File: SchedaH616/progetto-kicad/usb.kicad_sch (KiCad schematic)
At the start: 11 parts, among them J801 903-131A1011D10100, U801 TPS2553DBVR, U802 USBLC6-2SC6

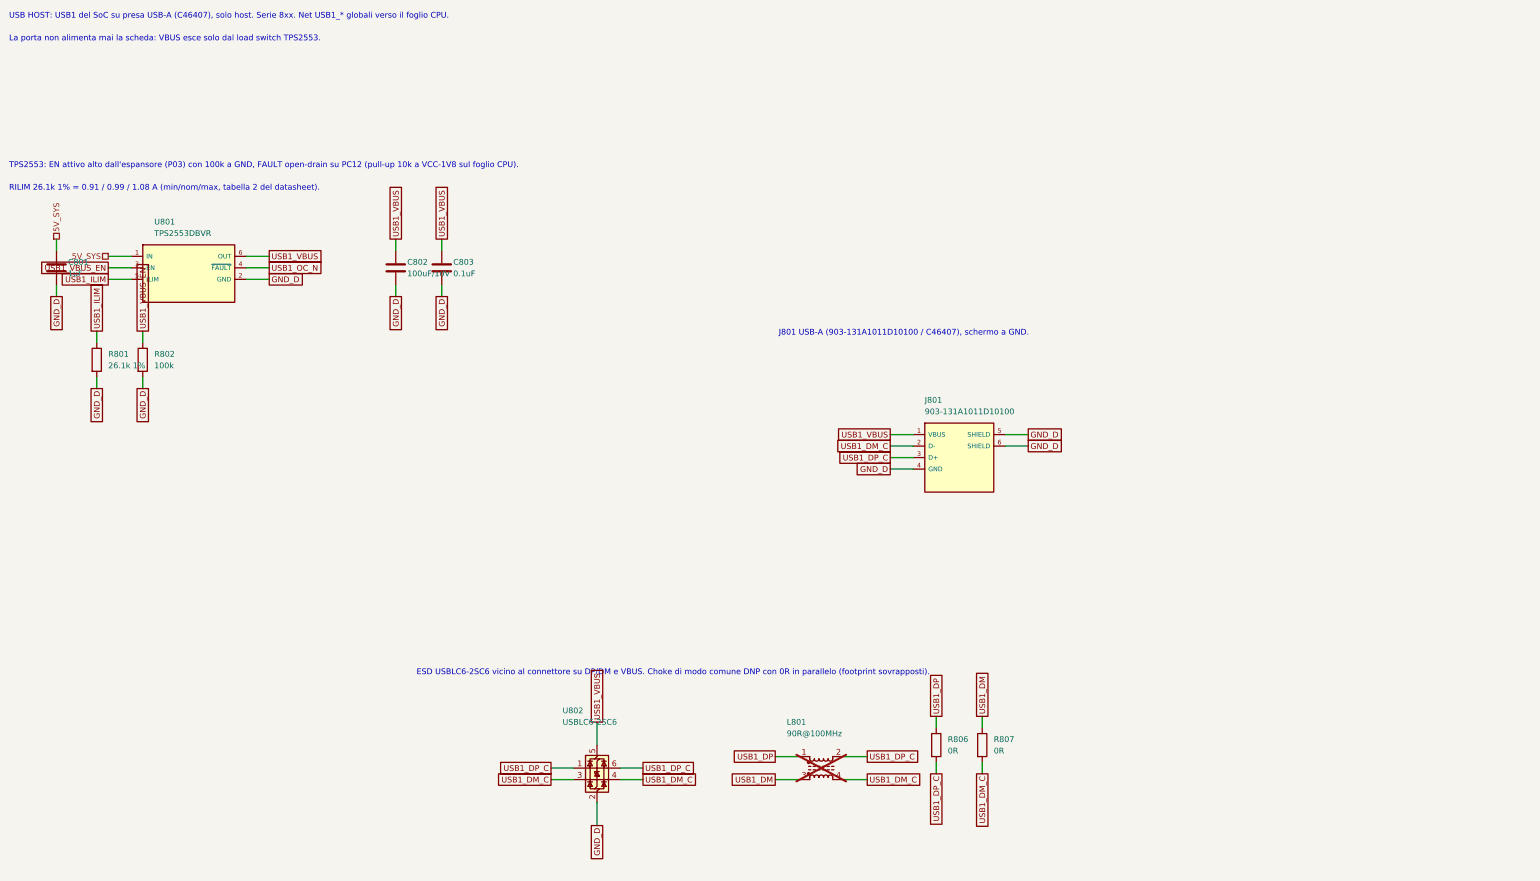
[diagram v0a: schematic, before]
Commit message: SchedaH616: placement PCB 50x70 a 6 strati e modifiche allo schema
PCB (solo placement, niente piste), generato da generatori/build_pcb.sh:
- 50 x 70 mm, smussi 3 mm, 4 fori NPTH 2.2 mm con keepout, 6 strati
- H616 al centro, LPDDR4 sul lato DRAM, AXP313A vicino alla CPU, eMMC vicino ai pin PC
- connettori sui bordi, U.FL Wi-Fi e SMA GNSS su lati opposti
- disaccoppiamento di H616 e LPDDR4 sul bottom sotto le sfere
- regole: piste 5 mil, via-in-pad 0.25/0.15 sotto l'H616
- DRC: 0 violazioni (solo collegamenti da fare), parità schema/PCB ok

Schema (modifiche approvate):
- LPDDR4 confermata come scelta definitiva
- USB host di nuovo su USB-C solo host (Rp 22k, USBLC6-2, TPS2553)
- jack 5 V diretto su IN1 del TPS2121, tolto l'SS54, TPS56637 in Eco-mode
- LDO AP2112K-1.8 (C176944) dedicato a VCCQ eMMC e VCC_PC
- ERC 0

Libreria H616.pretty: serigrafia sui pad tolta, pioli di centraggio NPTH.

Co-Authored-By: Claude Opus 5.5 (1M context) <noreply@anthropic.com>
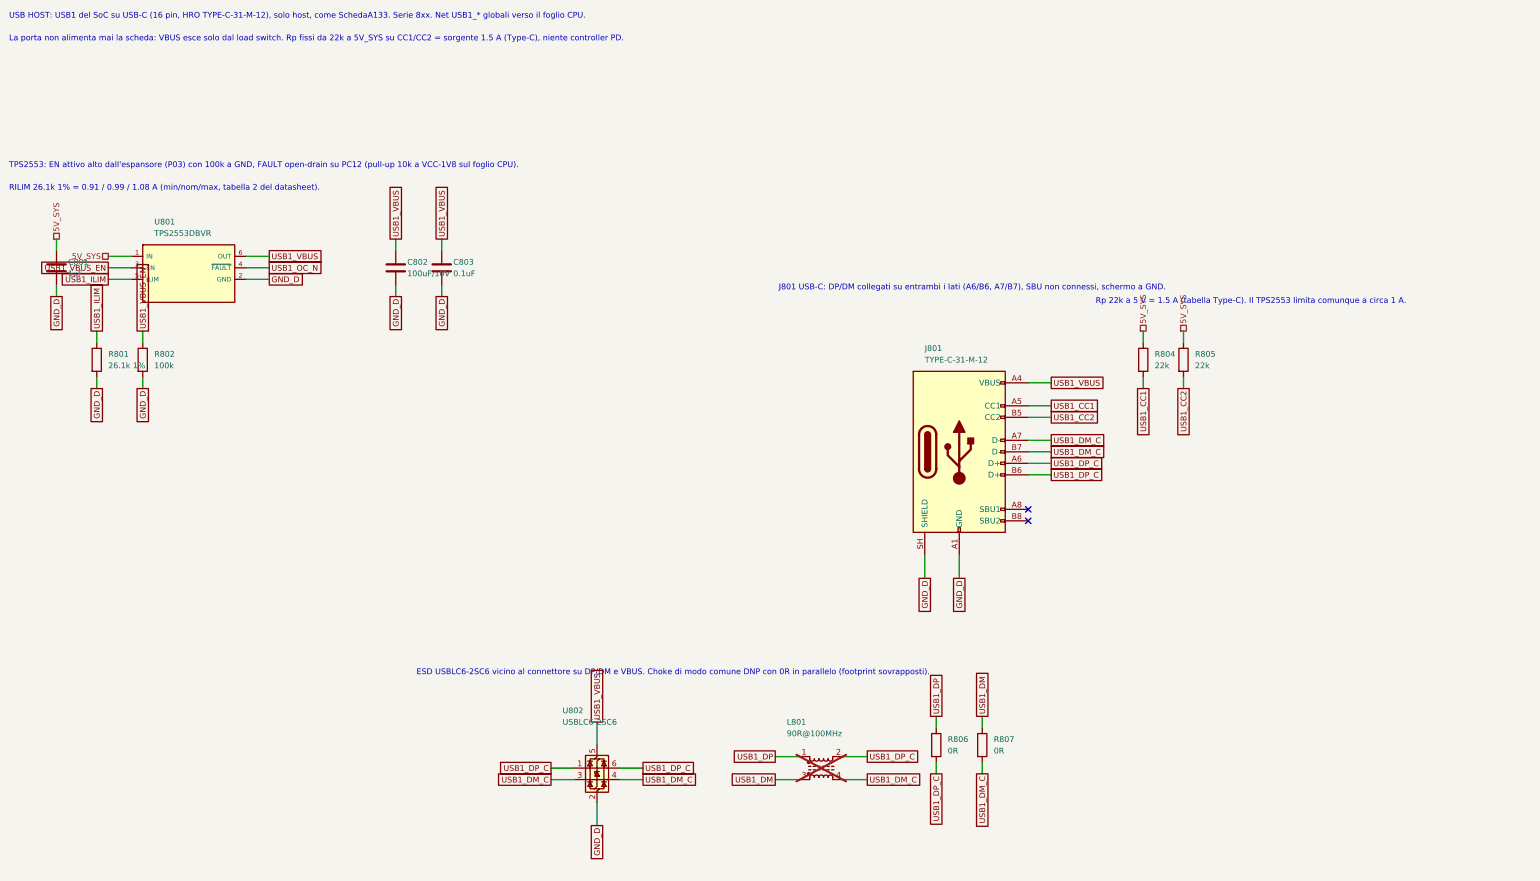
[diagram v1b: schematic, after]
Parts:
- removed J801: 903-131A1011D10100, H616:USB-A-TH_C46407, symbol H616:USB_A_C46407
- added J801: TYPE-C-31-M-12, Connector_USB:USB_C_Receptacle_HRO_TYPE-C-31-M-12, symbol Connector:USB_C_Receptacle_USB2.0_16P
- added R804, R805: 22k, Resistor_SMD:R_0402_1005Metric, symbol Device:R
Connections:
- net 5V_SYS: now also R804.1, R805.1
- net GND_D: now also J801.A1 (GND), J801.A12 (GND), J801.B1 (GND), J801.B12 (GND), J801.SH (SHIELD)
- net USB1_DM_C: now also J801.A7 (D-), J801.B7 (D-)
- net USB1_DP_C: now also J801.A6 (D+), J801.B6 (D+)
- net USB1_VBUS: now also J801.A4 (VBUS), J801.A9 (VBUS), J801.B4 (VBUS), J801.B9 (VBUS)
- new net USB1_CC1: J801.A5 (CC1), R804.2
- new net USB1_CC2: J801.B5 (CC2), R805.2
- no-connect marks 0 -> 2
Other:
- note added: "J801 USB-C: DP/DM collegati su entrambi i lati (A6/B6, A7/B7), SBU non connessi, schermo a GND."
- note added: "La porta non alimenta mai la scheda: VBUS esce solo dal load switch. Rp fissi da 22k a 5V_SYS su CC1/CC2 = sorgente 1.5 A (Type-C), niente controller PD."
- note added: "Rp 22k a 5 V = 1.5 A (tabella Type-C). Il TPS2553 limita comunque a circa 1 A."
- note added: "USB HOST: USB1 del SoC su USB-C (16 pin, HRO TYPE-C-31-M-12), solo host, come SchedaA133. Serie 8xx. Net USB1_* globali verso il foglio CPU."
- note removed: "J801 USB-A (903-131A1011D10100 / C46407), schermo a GND."
- note removed: "La porta non alimenta mai la scheda: VBUS esce solo dal load switch TPS2553."
- note removed: "USB HOST: USB1 del SoC su presa USB-A (C46407), solo host. Serie 8xx. Net USB1_* globali verso il foglio CPU."

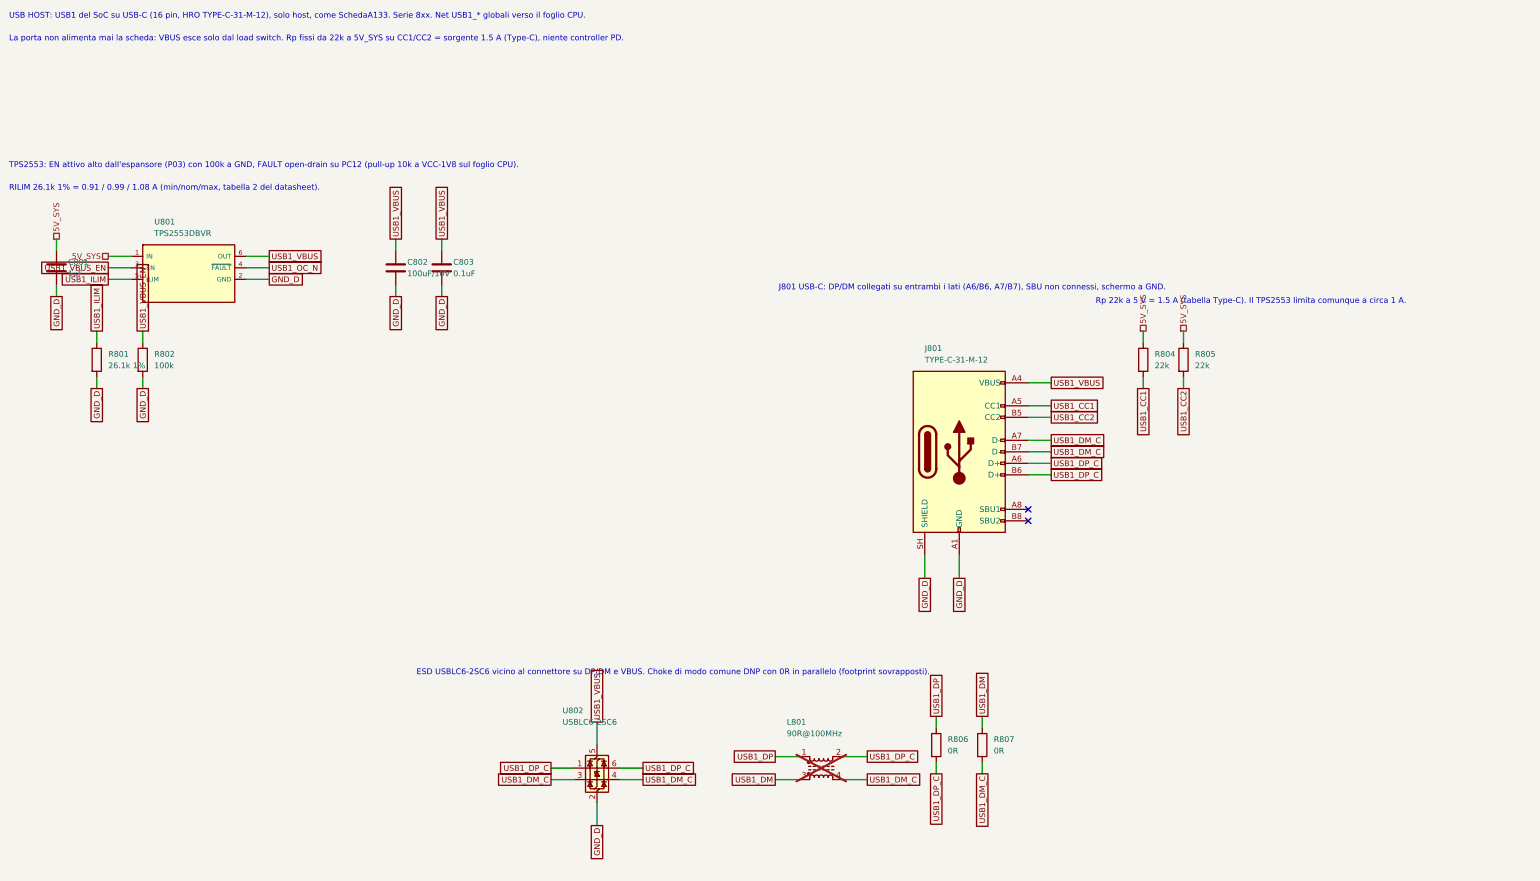
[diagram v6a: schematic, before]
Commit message: SchedaH616: RK3568 + RK809-5 + TCS4525 + DDR4, placement 50x70
- SoC Allwinner H616 -> Rockchip RK3568 (FCBGA636L, LCSC C2938930): ball map dal pinout
  Rockchip V1.1, verificata sulla tabella 2-1 del datasheet V1.2 (636/636); footprint
  generato (gen_fp.py), confrontato con EasyEDA C2938930
- PMIC AXP313A -> RK809-5 (C2939628) come Rockchip AIoT REF V1.1 / ROCK 3A; TCS4525 per
  VDD_CPU su I2C0 (0x1C); BUCK4 su VDD_NPU (sull'RK809-5 parte spento: non puo' fare il 3.3 V)
- LPDDR4 -> DDR4 x16 K4AAG165WA-BCWE (C2920140) sul canale A, point-to-point, niente VTT,
  VPP da AP2112K-2.5, ZQ 240R, DDR_RZQ del SoC 120R (Hardware Design Guide)
- eMMC su EMMC 8 bit (VCCIO2 1.8 V), microSD su SDMMC0, AP6256 su SDMMC2 + UART8,
  RTL8211F su GMAC0 RGMII (22R TX al SoC e RX al PHY), console UART2_M0, USB-C su OTG0
- Recovery su SARADC_VIN0, reset sulla rete RESETn; TCA6416A tolto
- Bus MIKILAB: BUS_POWER su SPI3_M1, MAIN su SPI2_M1 (CS del DAC su cs-gpios)
- progetto rinominato SchedaRK3568, libreria di progetto Scheda; script portabili Linux/macOS
- ERC 0, parita' 0, DRC 0 (solo collegamenti da fare); placement 439/439

Co-Authored-By: Claude Opus 5.5 (1M context) <noreply@anthropic.com>
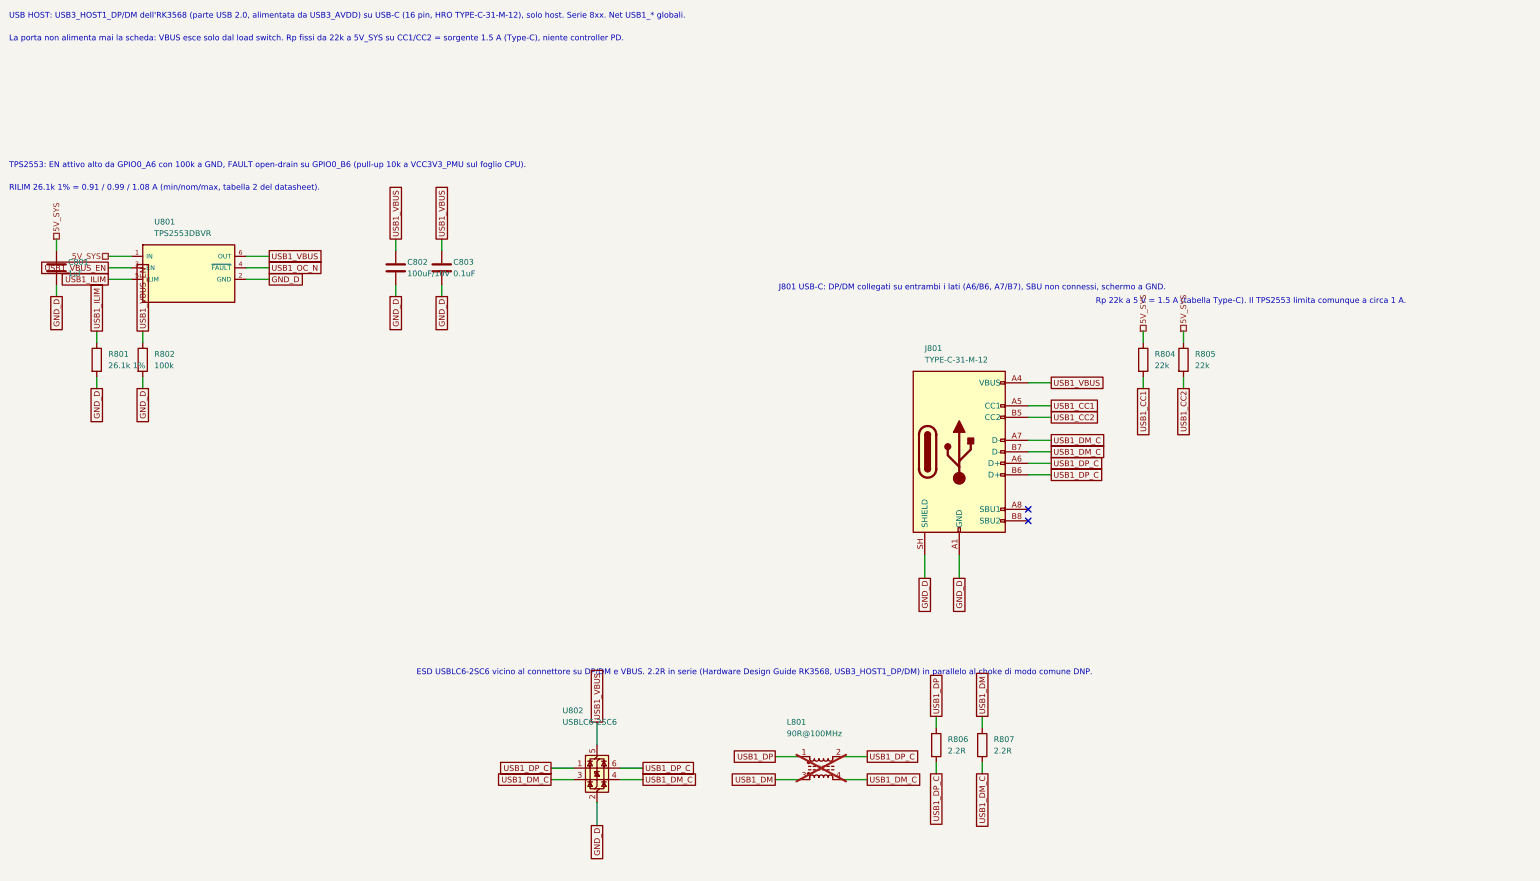
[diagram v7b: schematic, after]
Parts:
- removed U801: TPS2553DBVR, Package_TO_SOT_SMD:SOT-23-6, symbol H616:TPS2553DBV
- added U801: TPS2553DBVR, Package_TO_SOT_SMD:SOT-23-6, symbol Scheda:TPS2553DBV
- R806, R807: value 0R -> 2.2R
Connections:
- net 5V_SYS: now also U801.1 (IN)
- net GND_D: now also U801.2 (GND)
- net USB1_ILIM: now also U801.5 (ILIM)
- net USB1_OC_N: now also U801.4 (~{FAULT})
- net USB1_VBUS: now also U801.6 (OUT)
- net USB1_VBUS_EN: now also U801.3 (EN)
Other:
- note added: "ESD USBLC6-2SC6 vicino al connettore su DP/DM e VBUS. 2.2R in serie (Hardware Design Guide RK3568, USB3_HOST1_DP/DM) in parallelo al choke di modo comune DNP."
- note added: "TPS2553: EN attivo alto da GPIO0_A6 con 100k a GND, FAULT open-drain su GPIO0_B6 (pull-up 10k a VCC3V3_PMU sul foglio CPU)."
- note added: "USB HOST: USB3_HOST1_DP/DM dell'RK3568 (parte USB 2.0, alimentata da USB3_AVDD) su USB-C (16 pin, HRO TYPE-C-31-M-12), solo host. Serie 8xx. Net USB1_* globali."
- note removed: "ESD USBLC6-2SC6 vicino al connettore su DP/DM e VBUS. Choke di modo comune DNP con 0R in parallelo (footprint sovrapposti)."
- note removed: "TPS2553: EN attivo alto dall'espansore (P03) con 100k a GND, FAULT open-drain su PC12 (pull-up 10k a VCC-1V8 sul foglio CPU)."
- note removed: "USB HOST: USB1 del SoC su USB-C (16 pin, HRO TYPE-C-31-M-12), solo host, come SchedaA133. Serie 8xx. Net USB1_* globali verso il foglio CPU."

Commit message: SchedaH616: componenti specifici dalla libreria MIKILAB
- simbolo e footprint MIKILAB per RK809-5, TCS4525, K4AAG165WA-BCWE, FEMDNN064G-C9A61,
  AP2112K-1.8TRG1, TPS56637RPAR, TPS2121RUXR, SY6280AAC, TPS563201DDCR, TPS2553DBVR,
  TYPE-C-31-M-12, FH12-30S-0.5SH, FPC-05F-28PH20, HR911130C, 25AA02E48T-I/OT, DM3AT-SF-PEJM5;
  simbolo MIKILAB per l'AP6256
- restano nella libreria di progetto: RK3568 (pad EasyEDA da 0.35 mm, niente fanout 5/5 mil),
  simbolo RTL8211F (quello MIKILAB ha pin di alimentazione nascosti), footprint AP6256 LGA-47,
  portapila BS-12; motivazioni in docs/scelte-progetto.md
- kilib.mik() carica simboli e footprint dalla libreria (variabile MIKILAB); matrice ERC:
  pin unspecified dei simboli EasyEDA OK
- netlist identica a 4ca35fc (439 componenti, 314 net); ERC 0, parita' 0, DRC 0 (solo
  collegamenti da fare); footprint corretti nella libreria MIKILAB 8b990c4

Co-Authored-By: Claude Opus 5.5 (1M context) <noreply@anthropic.com>
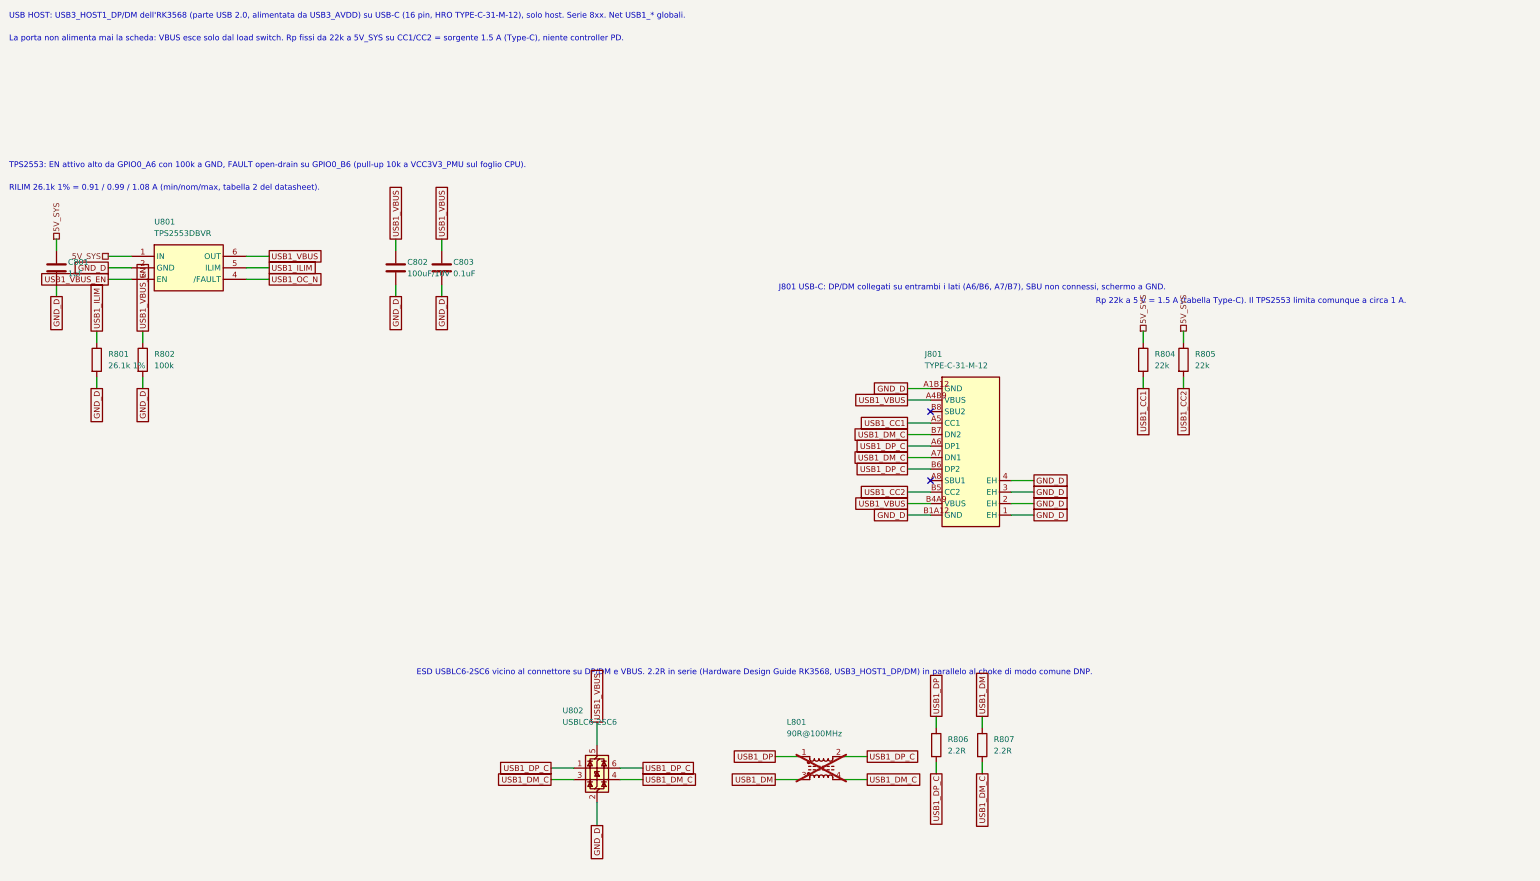
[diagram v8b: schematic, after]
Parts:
- removed J801: TYPE-C-31-M-12, Connector_USB:USB_C_Receptacle_HRO_TYPE-C-31-M-12, symbol Connector:USB_C_Receptacle_USB2.0_16P
- removed U801: TPS2553DBVR, Package_TO_SOT_SMD:SOT-23-6, symbol Scheda:TPS2553DBV
- added J801: TYPE-C-31-M-12, MIKILAB_TYPE_C_31_M_12:USB-C_SMD-TYPE-C-31-M-12_1, symbol MIKILAB_TYPE_C_31_M_12:TYPE-C-31-M-12
- added U801: TPS2553DBVR, MIKILAB_TPS2553DBVR:TPS2553DBVR_SOT-23-6_L2.9-W1.6-P0.95-LS2.8-BR, symbol MIKILAB_TPS2553DBVR:TPS2553DBVR
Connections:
- net 5V_SYS: now also U801.1 (IN)
- net GND_D: now also J801.1 (EH), J801.2 (EH), J801.3 (EH), J801.4 (EH), J801.A1B12 (GND), J801.B1A12 (GND), U801.2 (GND)
- net USB1_CC1: now also J801.A5 (CC1)
- net USB1_CC2: now also J801.B5 (CC2)
- net USB1_DM_C: now also J801.A7 (DN1), J801.B7 (DN2)
- net USB1_DP_C: now also J801.A6 (DP1), J801.B6 (DP2)
- net USB1_ILIM: now also U801.5 (ILIM)
- net USB1_OC_N: now also U801.4 (/FAULT)
- net USB1_VBUS: now also J801.A4B9 (VBUS), J801.B4A9 (VBUS), U801.6 (OUT)
- net USB1_VBUS_EN: now also U801.3 (EN)
